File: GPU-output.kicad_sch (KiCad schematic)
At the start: 19 parts

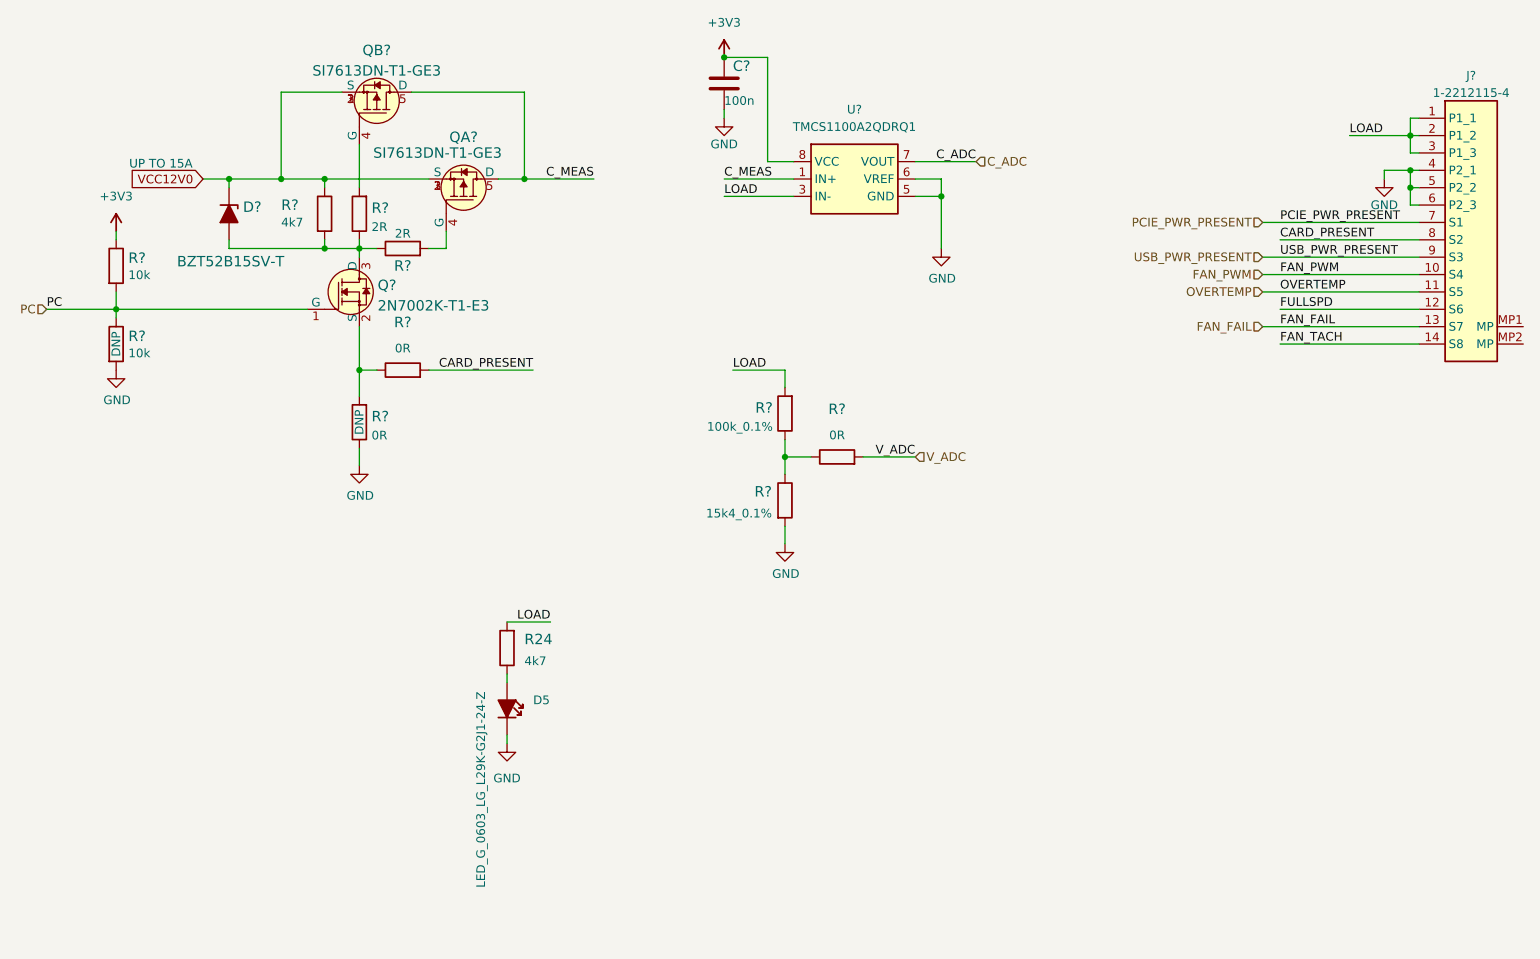
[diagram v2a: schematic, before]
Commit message: Repleace non standard components in connectors and ftdi and power
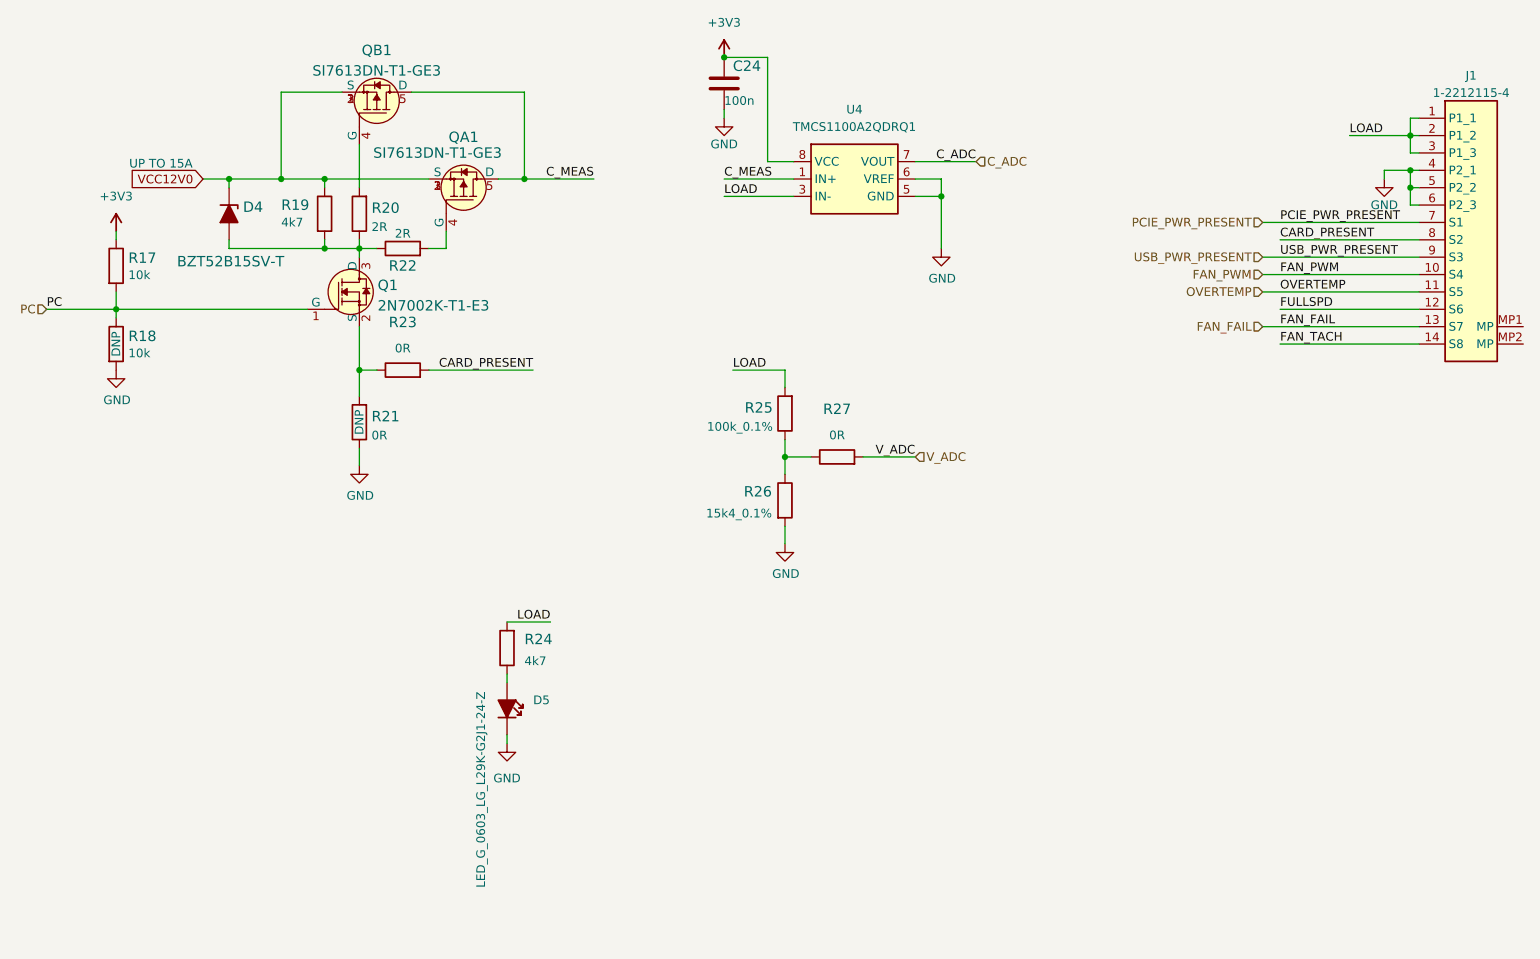
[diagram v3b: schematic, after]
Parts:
- gave numbers to parts that had none: 17
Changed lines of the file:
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@@
   (symbol (lib_id "antmicroResistors0402:R_100k_0.1%_0402") (at 140.97 87.63 90) (unit 1)
     (in_bom yes) (on_board yes) (fields_autoplaced)
-    (property "Reference" "R?" (id 0) (at 139.1921 86.7954 90)
+    (property "Reference" "R25" (id 0) (at 139.1921 86.7954 90)
       (effects (font (size 1.524 1.524)) (justify left))
     )
@@
   (symbol (lib_id "antmicroResistors0402:R_10k_0402") (at 43.18 66.04 270) (unit 1)
     (in_bom yes) (on_board yes)
-    (property "Reference" "R?" (id 0) (at 44.958 64.897 90)
+    (property "Reference" "R17" (id 0) (at 44.958 64.897 90)
       (effects (font (size 1.524 1.524)) (justify left))
     )
@@
   (symbol (lib_id "antmicroResistors0402:R_15k4_0.1%_0402") (at 140.97 100.33 270) (unit 1)
     (in_bom yes) (on_board yes)
-    (property "Reference" "R?" (id 0) (at 139.065 99.0601 90)
+    (property "Reference" "R26" (id 0) (at 139.065 99.0601 90)
       (effects (font (size 1.524 1.524)) (justify right))
     )
@@
   (symbol (lib_id "antmicroResistors0402:R_2R_0402") (at 78.74 58.42 90) (unit 1)
     (in_bom yes) (on_board yes) (fields_autoplaced)
-    (property "Reference" "R?" (id 0) (at 80.518 57.5854 90)
+    (property "Reference" "R20" (id 0) (at 80.518 57.5854 90)
       (effects (font (size 1.524 1.524)) (justify right))
     )
@@
   (symbol (lib_id "antmicroTransistorsFETsMOSFETsSingle:2N7002K-T1-E3") (at 78.74 69.85 0) (unit 1)
     (in_bom yes) (on_board yes) (fields_autoplaced)
-    (property "Reference" "Q?" (id 0) (at 81.407 68.8738 0)
+    (property "Reference" "Q1" (id 0) (at 81.407 68.8738 0)
       (effects (font (size 1.524 1.524)) (justify left))
     )
@@
   (symbol (lib_id "antmicropower:GND") (at 78.74 95.25 0) (unit 1)
     (in_bom yes) (on_board yes)
-    (property "Reference" "#PWR?" (id 0) (at 78.74 101.6 0)
+    (property "Reference" "#PWR043" (id 0) (at 78.74 101.6 0)
       (effects (font (size 1.27 1.27)) hide)
     )
@@
   (symbol (lib_id "antmicroCapacitors0402:C_100n_0402") (at 132.08 39.37 0) (unit 1)
     (in_bom yes) (on_board yes)
-    (property "Reference" "C?" (id 0) (at 133.35 36.83 0)
+    (property "Reference" "C24" (id 0) (at 133.35 36.83 0)
       (effects (font (size 1.524 1.524)) (justify left))
     )
@@
   (symbol (lib_id "antmicroResistors0402:R_10k_0402") (at 43.18 77.47 270) (unit 1)
     (in_bom yes) (on_board yes)
-    (property "Reference" "R?" (id 0) (at 44.958 76.327 90)
+    (property "Reference" "R18" (id 0) (at 44.958 76.327 90)
       (effects (font (size 1.524 1.524)) (justify left))
     )
@@
   (symbol (lib_id "antmicroB2bConnectors:Conn_1-2212115-4") (at 233.68 44.45 0) (unit 1)
     (in_bom yes) (on_board yes) (fields_autoplaced)
-    (property "Reference" "J?" (id 0) (at 241.3 38.225 0)
+    (property "Reference" "J1" (id 0) (at 241.3 38.225 0)
       (effects (font (size 1.27 1.27) (thickness 0.15)))
     )
@@
   (symbol (lib_id "antmicropower:GND") (at 163.83 63.5 0) (unit 1)
     (in_bom yes) (on_board yes)
-    (property "Reference" "#PWR?" (id 0) (at 163.83 69.85 0)
+    (property "Reference" "#PWR048" (id 0) (at 163.83 69.85 0)
       (effects (font (size 1.27 1.27)) hide)
     )
@@
   (symbol (lib_id "antmicroTransistorsFETsMOSFETsSingle:SI7613DN-T1-GE3") (at 93.98 53.34 270) (mirror x) (unit 1)
     (in_bom yes) (on_board yes)
-    (property "Reference" "QA?" (id 0) (at 93.98 47.2239 90)
+    (property "Reference" "QA1" (id 0) (at 93.98 47.2239 90)
       (effects (font (size 1.524 1.524)))
     )
@@
   (symbol (lib_id "antmicroPowerMeasurement:TMCS1100A2-Q1") (at 142.24 50.8 0) (unit 1)
     (in_bom yes) (on_board yes) (fields_autoplaced)
-    (property "Reference" "U?" (id 0) (at 151.13 43.18 0)
+    (property "Reference" "U4" (id 0) (at 151.13 43.18 0)
       (effects (font (size 1.27 1.27) (thickness 0.15)))
     )
@@
   (symbol (lib_id "antmicroResistors0402:R_0R_0402") (at 85.09 81.28 0) (unit 1)
     (in_bom yes) (on_board yes) (fields_autoplaced)
-    (property "Reference" "R?" (id 0) (at 85.09 74.295 0)
+    (property "Reference" "R23" (id 0) (at 85.09 74.295 0)
       (effects (font (size 1.524 1.524)))
     )
@@
   (symbol (lib_id "antmicroDiodesZenerSingle:BZT52B15SV-T") (at 59.69 58.42 270) (unit 1)
     (in_bom yes) (on_board yes)
-    (property "Reference" "D?" (id 0) (at 61.722 57.4438 90)
+    (property "Reference" "D4" (id 0) (at 61.722 57.4438 90)
       (effects (font (size 1.524 1.524)) (justify left))
     )
@@
   (symbol (lib_id "antmicroResistors0402:R_2R_0402") (at 85.09 63.5 0) (unit 1)
     (in_bom yes) (on_board yes)
-    (property "Reference" "R?" (id 0) (at 85.09 66.04 0)
+    (property "Reference" "R22" (id 0) (at 85.09 66.04 0)
       (effects (font (size 1.524 1.524)))
     )
@@
   (symbol (lib_id "antmicropower:GND") (at 140.97 106.68 0) (unit 1)
     (in_bom yes) (on_board yes)
-    (property "Reference" "#PWR?" (id 0) (at 140.97 113.03 0)
+    (property "Reference" "#PWR047" (id 0) (at 140.97 113.03 0)
       (effects (font (size 1.27 1.27)) hide)
     )
@@
   (symbol (lib_id "antmicroResistors0402:R_4k7_0402") (at 73.66 58.42 270) (unit 1)
     (in_bom yes) (on_board yes)
-    (property "Reference" "R?" (id 0) (at 67.31 57.15 90)
+    (property "Reference" "R19" (id 0) (at 67.31 57.15 90)
       (effects (font (size 1.524 1.524)) (justify left))
     )
@@
   (symbol (lib_id "antmicroResistors0402:R_0R_0402") (at 148.59 93.98 0) (unit 1)
     (in_bom yes) (on_board yes) (fields_autoplaced)
-    (property "Reference" "R?" (id 0) (at 148.59 86.995 0)
+    (property "Reference" "R27" (id 0) (at 148.59 86.995 0)
       (effects (font (size 1.524 1.524)))
     )
@@
   (symbol (lib_id "antmicropower:GND") (at 43.18 81.28 0) (unit 1)
     (in_bom yes) (on_board yes)
-    (property "Reference" "#PWR?" (id 0) (at 43.18 87.63 0)
+    (property "Reference" "#PWR042" (id 0) (at 43.18 87.63 0)
       (effects (font (size 1.27 1.27)) hide)
     )
@@
   (symbol (lib_id "antmicropower:GND") (at 228.6 53.34 0) (unit 1)
     (in_bom yes) (on_board yes)
-    (property "Reference" "#PWR?" (id 0) (at 228.6 59.69 0)
+    (property "Reference" "#PWR049" (id 0) (at 228.6 59.69 0)
       (effects (font (size 1.27 1.27)) hide)
     )
@@
   (symbol (lib_id "antmicroTransistorsFETsMOSFETsSingle:SI7613DN-T1-GE3") (at 81.28 40.64 270) (mirror x) (unit 1)
     (in_bom yes) (on_board yes) (fields_autoplaced)
-    (property "Reference" "QB?" (id 0) (at 81.28 34.5239 90)
+    (property "Reference" "QB1" (id 0) (at 81.28 34.5239 90)
       (effects (font (size 1.524 1.524)))
     )
@@
   (symbol (lib_id "antmicropower:GND") (at 132.08 44.45 0) (unit 1)
     (in_bom yes) (on_board yes)
-    (property "Reference" "#PWR?" (id 0) (at 132.08 50.8 0)
+    (property "Reference" "#PWR046" (id 0) (at 132.08 50.8 0)
       (effects (font (size 1.27 1.27)) hide)
     )
@@
   (symbol (lib_id "antmicroResistors0402:R_0R_0402") (at 78.74 88.9 90) (unit 1)
     (in_bom yes) (on_board yes)
-    (property "Reference" "R?" (id 0) (at 80.518 88.0654 90)
+    (property "Reference" "R21" (id 0) (at 80.518 88.0654 90)
       (effects (font (size 1.524 1.524)) (justify right))
     )

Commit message: Replace outpouts components
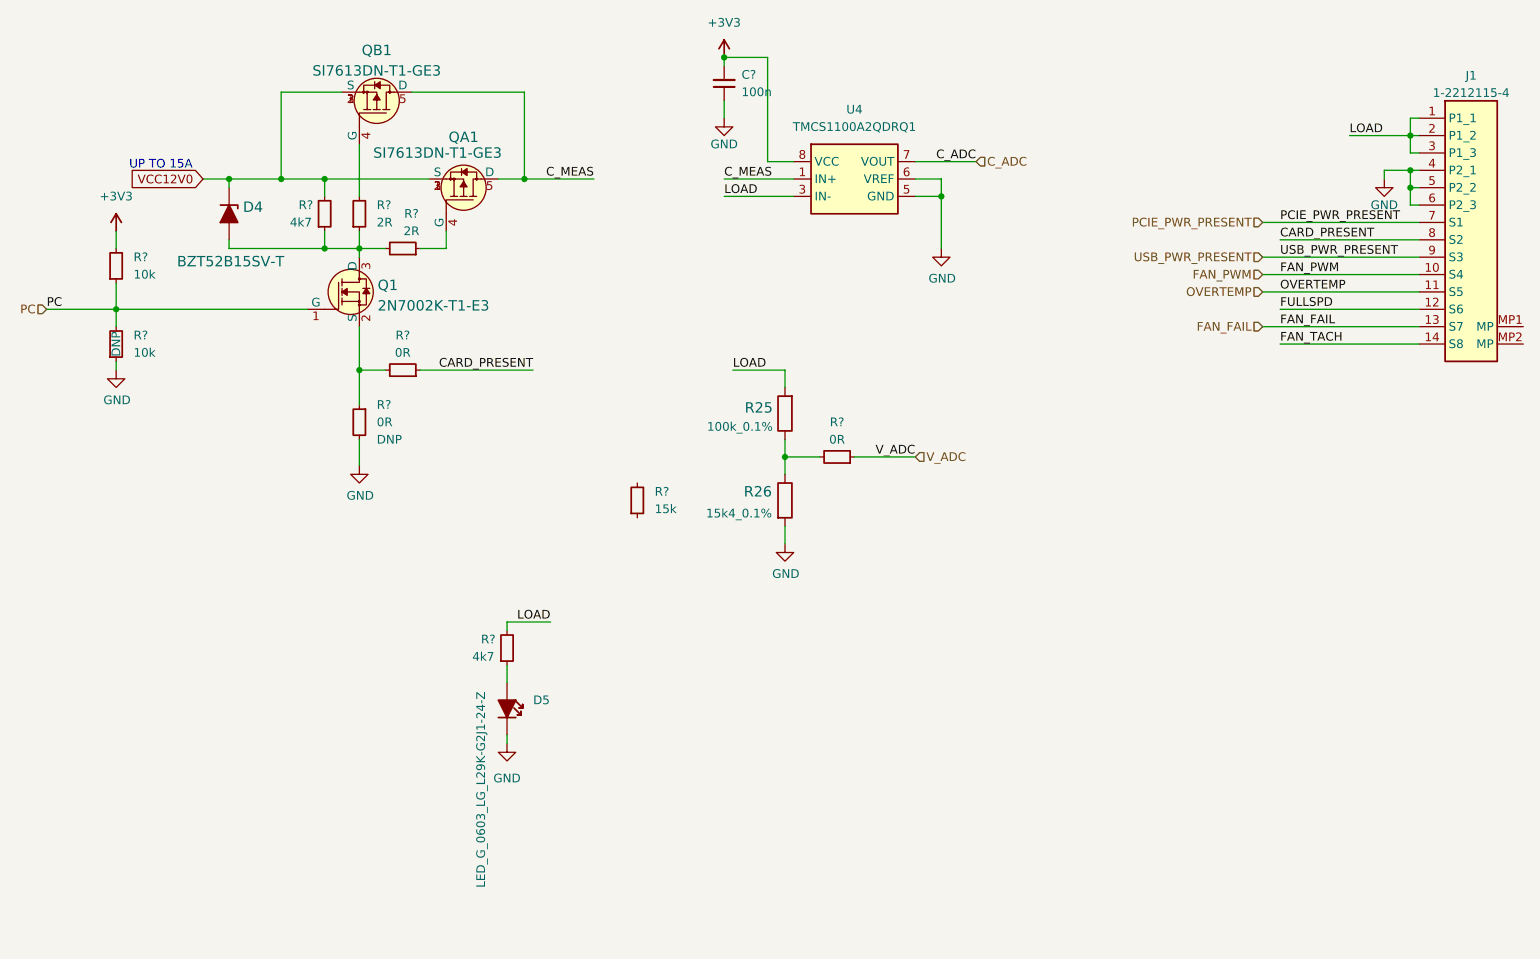
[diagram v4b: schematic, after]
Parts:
- removed C24: C_100n_0402, antmicro-footprints:C_0402_1005Metric, symbol antmicroCapacitors0402:C_100n_0402
- removed R17, R18: R_10k_0402, antmicro-footprints:R_0402_1005Metric, symbol antmicroResistors0402:R_10k_0402
- removed R19: R_4k7_0402, antmicro-footprints:R_0402_1005Metric, symbol antmicroResistors0402:R_4k7_0402
- removed R20, R22: R_2R_0402, antmicro-footprints:0402-res, symbol antmicroResistors0402:R_2R_0402
- removed R21, R23, R27: R_0R_0402, antmicro-footprints:R_0402_1005Metric, symbol antmicroResistors0402:R_0R_0402
- removed R24: R_4k7_0603, antmicro-footprints:R_0603_1608Metric, symbol antmicroResistors0603:R_4k7_0603
- added C?: C_100n_0402, antmicro-footprints:C_0402_1005Metric, symbol antmicroCapacitors0402:C_100n_0402
- added R? (x3): R_0R_0402, antmicro-footprints:R_0402_1005Metric, symbol antmicroResistors0402:R_0R_0402
- added R? (x2): R_4k7_0402, antmicro-footprints:R_0402_1005Metric, symbol antmicroResistors0402:R_4k7_0402
- added R? (x2): R_10k_0402, antmicro-footprints:R_0402_1005Metric, symbol antmicroResistors0402:R_10k_0402
- added R?: R_15k_0.1%_0402, antmicro-footprints:R_0402_1005Metric, symbol antmicroResistors0402:R_15k_0.1%_0402
- added R? (x2): R_2R_0402, antmicro-footprints:R_0402_1005Metric, symbol antmicroResistors0402:R_2R_0402
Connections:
- net +3V3: now also C?.2, R?.2
- net CARD_PRESENT: now also R?.1
- net GND: now also C?.1, R?.1, R?.2
- net LOAD: now also R?.2
- net PC: now also R?.1, R?.2
- net VCC12V0: now also R?.2
- net V_ADC: now also R?.1
- net at R25.1, R26.1: now also R?.2
- net at D4.A, Q1.3 (D): now also R?.1, R?.1, R?.2
- net at QB1.4 (G): now also R?.2
- net at D5.1: now also R?.1
- net at Q1.2 (S): now also R?.1, R?.2
- net at QA1.4 (G): now also R?.1
